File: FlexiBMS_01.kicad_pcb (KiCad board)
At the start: 4 copper layers, 65 x 35 mm, 200 parts, among them J1 Conn_02x08_Odd_Even, J2 USB_OTG, J3 Conn_01x05, J4 JST_XH-04, J5 JST_XH-04, J6 JST_XH-13, J7 Conn_01x03, Q1 DMP6023LE-13, Q10 Q_PMOS_GSD, Q11 Q_PMOS_GSD, Q12 Q_PMOS_GSD, Q13 Q_PMOS_GSD, Q14 Q_PMOS_GSD, Q15 Q_PMOS_GSD, Q16 Q_PMOS_GSD, Q17 BSZ100N06NSATMA1, Q2 DMN55D0UT-7, Q3 PMV50XPR, Q4 PMV50XPR, Q5 Q_PMOS_GSD, Q6 Q_PMOS_GSD, Q7 Q_PMOS_GSD, Q8 Q_PMOS_GSD, Q9 Q_PMOS_GSD, SW1 SW_Push, SW2 SW_Push, U1 AP2210N-3.3, U2 STM32F070CBT6, U3 LTC6803-3, U4 MAX17502, U5 ISL28022, U6 LTC3873, U7 MAX5215, Y1 8MHz

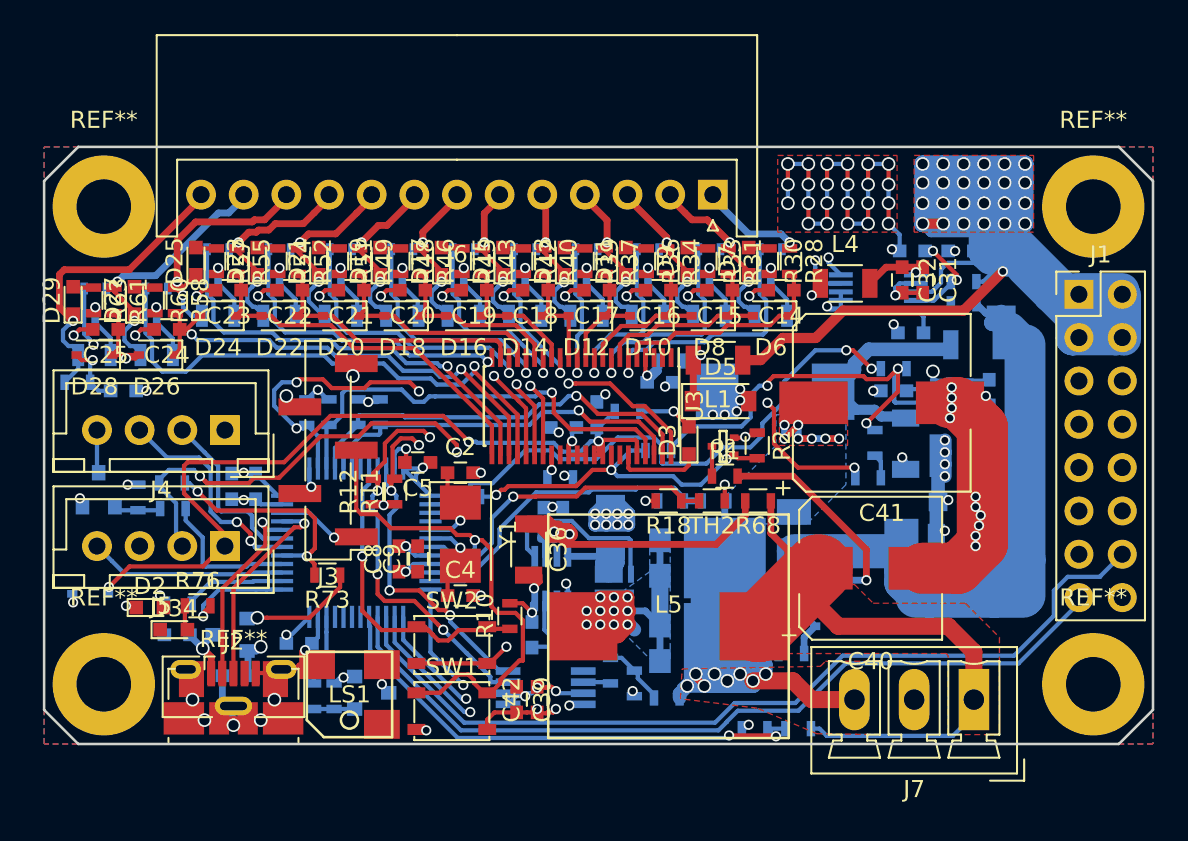
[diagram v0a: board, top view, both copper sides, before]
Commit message: 0.1 Version finalized Silkscreen has been optimized, gerber files have been generated and boards have been ordered
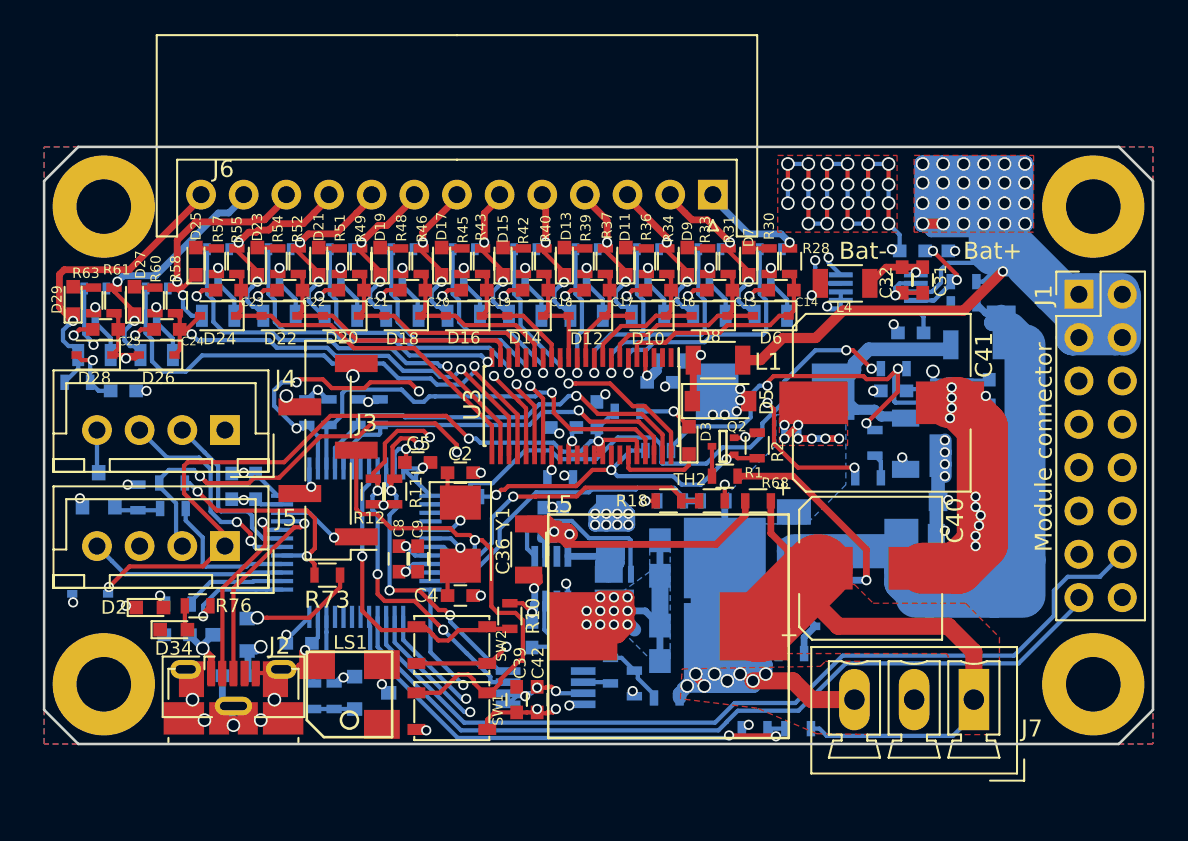
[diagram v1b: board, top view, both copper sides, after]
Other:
- net class Default: clearance 0.19 -> 0.2
- rule trace_clearance: 0.19 -> 0.2
- board text added: "+"
- board text added: "-"
- board text added: "0"
- board text added: "1"
- board text added: "10"
- board text added: "11"
- board text added: "12"
- board text added: "2"
- board text added: "3"
- board text added: "4"
- board text added: "5"
- board text added: "6"
- board text added: "7"
- board text added: "8"
- board text added: "9"
- board text added: "Bat+"
- board text added: "Bat-"
- board text added: "Boost+"
- board text added: "Bulk+"
- board text added: "FlexiBMS 0.1"
- board text added: "GND"
- board text added: "Module connector"
- board text added: "simo sihvonen 25022018"
